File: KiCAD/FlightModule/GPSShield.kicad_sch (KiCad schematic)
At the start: 6 parts

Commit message: コンデンサの容量耐圧が不明なため後ほど調べる
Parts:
- added 1: ~, MKRGPSShield_V4.0:BATT-HOLDER_12MM, symbol MKRGPSShield_V4.0-eagle-import:Arduino-connectors_BATT-HOLDER_12MM
- added C1: ~, MKRGPSShield_V4.0:0402-1005X55N, symbol MKRGPSShield_V4.0-eagle-import:Arduino-rcl_C-0402
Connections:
- net GND: now also 1.P$1 (-), C1.2
- net at IC2.3 (V_BCKP): now also 1.P$2 (+), C1.1

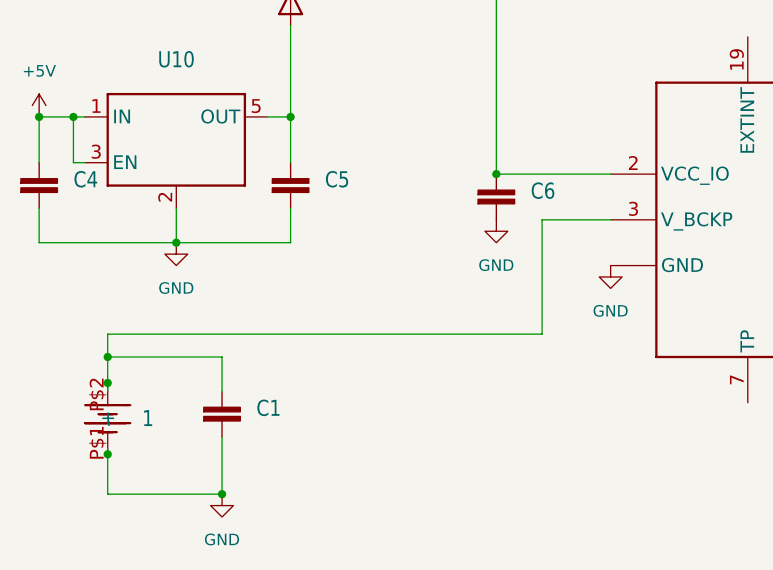
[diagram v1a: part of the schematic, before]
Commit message: MKR周りの配線完了
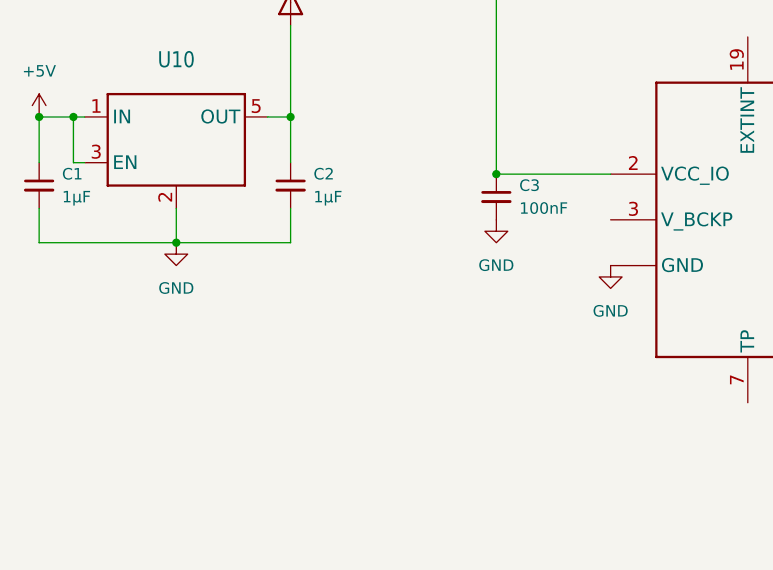
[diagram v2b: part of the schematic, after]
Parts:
- removed 1: ~, MKRGPSShield_V4.0:BATT-HOLDER_12MM, symbol MKRGPSShield_V4.0-eagle-import:Arduino-connectors_BATT-HOLDER_12MM
- removed C1, C4, C5, C6: ~, MKRGPSShield_V4.0:0402-1005X55N, symbol MKRGPSShield_V4.0-eagle-import:Arduino-rcl_C-0402
- added C1, C2: 1μF, symbol Device:C_Small
- added C3: 100nF, symbol Device:C_Small
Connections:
- net +5V: now also C1.1
- net GND: now also C1.2, C2.2, C3.2
- net at D6.2 (A2), U10.5 (OUT): now also C2.1
- net at D6.3 (K), IC2.17 (VCC), IC2.2 (VCC_IO): now also C3.1

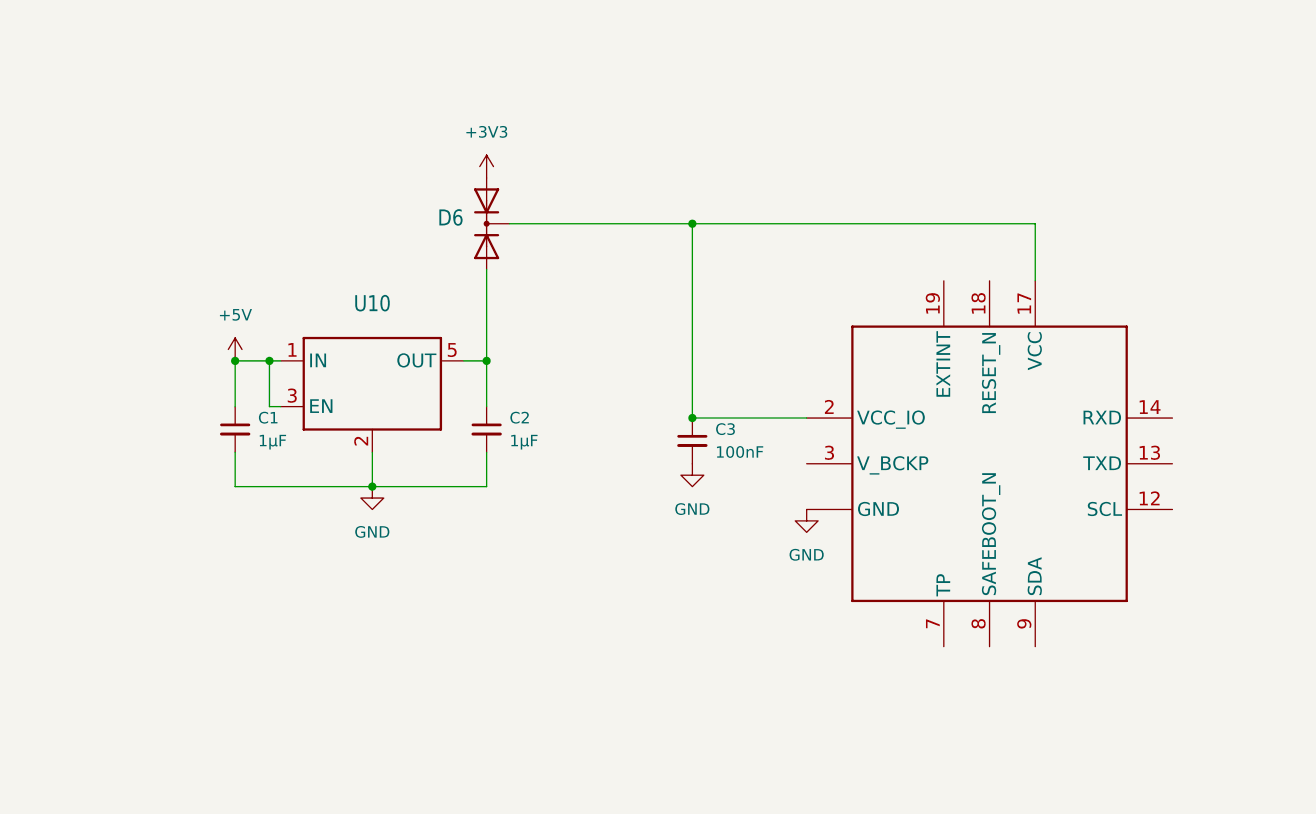
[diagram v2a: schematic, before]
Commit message: GPSShieldの部分完了
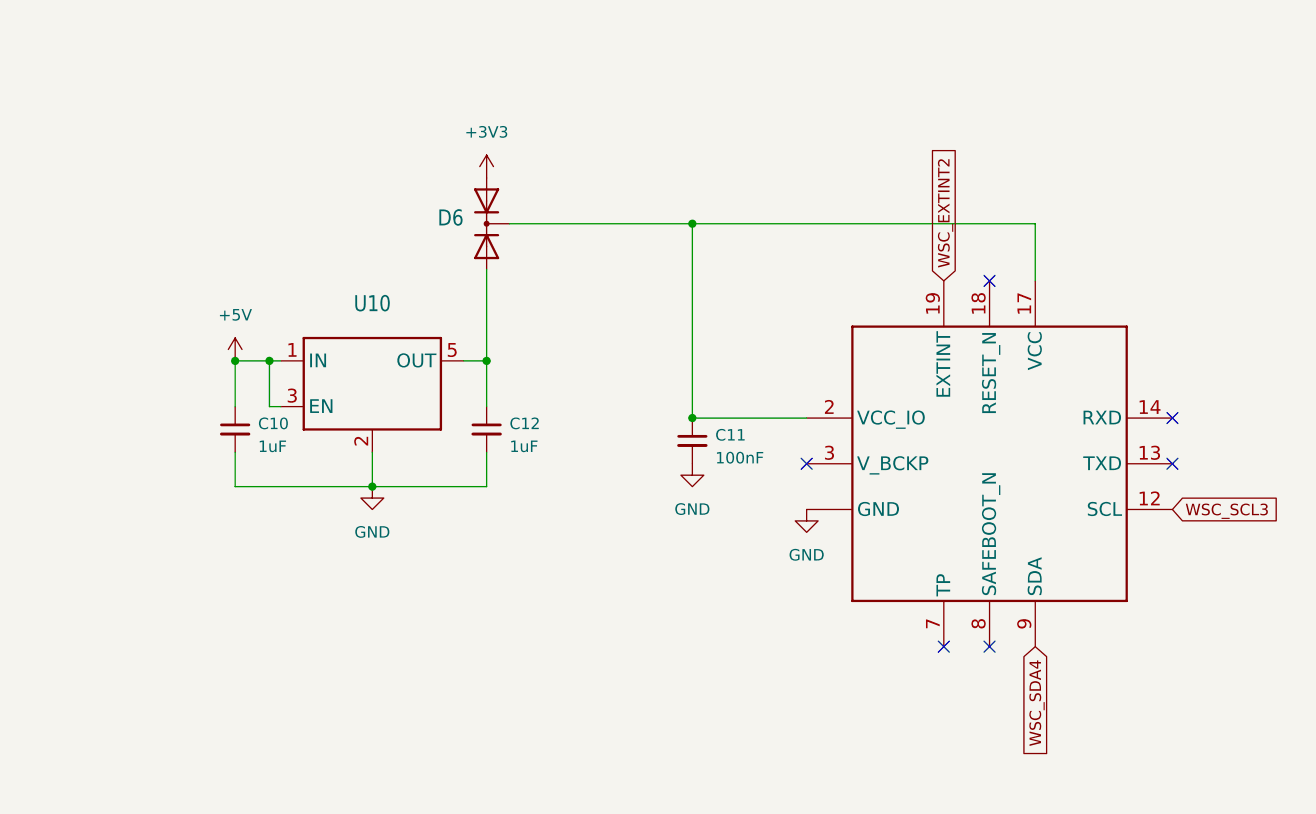
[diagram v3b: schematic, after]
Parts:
- removed C1, C2: 1μF, symbol Device:C_Small
- removed C3: 100nF, symbol Device:C_Small
- added C10, C12: 1uF, Capacitor_SMD:C_1206_3216Metric_Pad1.33x1.80mm_HandSolder, symbol Device:C_Small
- added C11: 100nF, Capacitor_SMD:C_1206_3216Metric_Pad1.33x1.80mm_HandSolder, symbol Device:C_Small
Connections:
- net +5V: now also C10.1
- net GND: now also C10.2, C11.2, C12.2
- net at D6.2 (A2), U10.5 (OUT): now also C12.1
- net at D6.3 (K), IC2.17 (VCC), IC2.2 (VCC_IO): now also C11.1
- net WSC_SCL3: now reaches IC2.12 (SCL)
- net WSC_EXTINT2: now reaches IC2.19 (EXTINT)
- net WSC_SDA4: now reaches IC2.9 (SDA)
- no-connect marks 0 -> 6

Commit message: GNSSモジュール，SAM-M8Qの回路図完成
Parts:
- removed C10, C12: 1uF, Capacitor_SMD:C_1206_3216Metric_Pad1.33x1.80mm_HandSolder, symbol Device:C_Small
- removed C11: 100nF, Capacitor_SMD:C_1206_3216Metric_Pad1.33x1.80mm_HandSolder, symbol Device:C_Small
- removed D6: ~, MKRGPSShield_V4.0:SOT65P210X110-3N, symbol MKRGPSShield_V4.0-eagle-import:Arduino-diodes_A2K_SOT-323
- removed IC2: ~, GPSShield:UBLOXLIB_SAM-M8Q, symbol MKRGPSShield_V4.0-eagle-import:SAM-M8Q
- removed U10: ~, MKRGPSShield_V4.0:SOT25, symbol MKRGPSShield_V4.0-eagle-import:AP2112K-3.3
- added C16, C17: 1uF, Capacitor_SMD:C_1206_3216Metric_Pad1.33x1.80mm_HandSolder, symbol Device:C_Small
- added R27: 100k, Resistor_SMD:R_0603_1608Metric_Pad0.98x0.95mm_HandSolder, symbol Device:R
- added R28: 0, Resistor_SMD:R_0603_1608Metric_Pad0.98x0.95mm_HandSolder, symbol Device:R
- added R29, R30: 4.7k, Resistor_SMD:R_0603_1608Metric_Pad0.98x0.95mm_HandSolder, symbol Device:R
- added U3: SAM-M8Q-0-10, TSRP_IC:MODULE_SAM-M8Q-0-10, symbol TSRP_IC:SAM-M8Q-0-10
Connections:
- net +3V3: now also C16.1, C17.1, R27.1, R28.1, R29.1, R30.1, U3.17 (VCC), U3.2 (VCC_IO)
- net GND: now also C16.2, C17.2, U3.1 (GND), U3.10 (GND), U3.11 (GND), U3.15 (GND), U3.16 (GND), U3.20 (GND), U3.4 (GND), U3.5 (GND), U3.6 (GND)
- new net: R28.2, U3.3 (V_BCKP)
- new net EXTINT_SAM-M8Q: U3.19 (EXTINT0)
- new net I2C_SCL: R29.2, U3.12 (SCL)
- new net I2C_SDA: R30.2, U3.9 (SDA)
- new net UART_RXD: R27.2, U3.14 (RXD)
- new net UART_TXD: U3.13 (TXD)
- no-connect marks 6 -> 2
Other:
- note added: "ジャンパ抵抗"

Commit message: 回路図8割完成
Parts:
- U3: footprint TSRP_IC:MODULE_SAM-M8Q-0-10 -> SAM-M8Q-0-10:MODULE_SAM-M8Q-0-10
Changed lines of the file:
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@@
 			)
 		)
-		(property "Footprint" "TSRP_IC:MODULE_SAM-M8Q-0-10"
+		(property "Footprint" "SAM-M8Q-0-10:MODULE_SAM-M8Q-0-10"
 			(at 104.14 68.58 0)
 			(effects
@@
 				(path "/3507137a-fdd7-4bc0-abe8-370b7c3b390e/5f21eb00-60ce-4306-a223-a9b9ec9552df"
 					(reference "#PWR062")
+					(unit 1)
+				)
+			)
+		)
+	)
+	(symbol
+		(lib_name "GND_2")
+		(lib_id "power:GND")
+		(at 93.98 93.98 0)
+		(unit 1)
+		(exclude_from_sim no)
+		(in_bom yes)
+		(on_board yes)
+		(dnp no)
+		(fields_autoplaced yes)
+		(property "Reference" "#PWR014"
+			(at 93.98 100.33 0)
+			(effects
+				(font
+					(size 1.27 1.27)
+				)
+				(hide yes)
+			)
+		)
+		(property "Value" "GND"
+			(at 93.98 99.06 0)
+			(effects
+				(font
+					(size 1.27 1.27)
+				)
+			)
+		)
+		(property "Footprint" ""
+			(at 93.98 93.98 0)
+			(effects
+				(font
+					(size 1.27 1.27)
+				)
+				(hide yes)
+			)
+		)
+		(property "Datasheet" ""
+			(at 93.98 93.98 0)
+			(effects
+				(font
+					(size 1.27 1.27)
+				)
+				(hide yes)
+			)
+		)
+		(property "Description" "Power symbol creates a global label with name \"GND\" , ground"
+			(at 93.98 93.98 0)
+			(effects
+				(font
+					(size 1.27 1.27)
+				)
+				(hide yes)
+			)
+		)
+		(pin "1"
+		)
+		(instances
+			(project "FlightModule"
+				(path "/3507137a-fdd7-4bc0-abe8-370b7c3b390e/5f21eb00-60ce-4306-a223-a9b9ec9552df"
+					(reference "#PWR014")
+					(unit 1)
+				)
+			)
+			(project "GPSShield"
+				(path "/e91f5324-b1bd-4996-81c2-18550b5297b9"
+					(reference "#PWR?")
 					(unit 1)
 				)
@@
 					(unit 1)
 				)
-			)
-		)
-	)
-	(symbol
-		(lib_name "GND_2")
-		(lib_id "power:GND")
-		(at 93.98 93.98 0)
-		(unit 1)
-		(exclude_from_sim no)
-		(in_bom yes)
-		(on_board yes)
-		(dnp no)
-		(fields_autoplaced yes)
-		(property "Reference" "#PWR014"
-			(at 93.98 100.33 0)
-			(effects
-				(font
-					(size 1.27 1.27)
-				)
-				(hide yes)
-			)
-		)
-		(property "Value" "GND"
-			(at 93.98 99.06 0)
-			(effects
-				(font
-					(size 1.27 1.27)
-				)
-			)
-		)
-		(property "Footprint" ""
-			(at 93.98 93.98 0)
-			(effects
-				(font
-					(size 1.27 1.27)
-				)
-				(hide yes)
-			)
-		)
-		(property "Datasheet" ""
-			(at 93.98 93.98 0)
-			(effects
-				(font
-					(size 1.27 1.27)
-				)
-				(hide yes)
-			)
-		)
-		(property "Description" "Power symbol creates a global label with name \"GND\" , ground"
-			(at 93.98 93.98 0)
-			(effects
-				(font
-					(size 1.27 1.27)
-				)
-				(hide yes)
-			)
-		)
-		(pin "1"
-		)
-		(instances
-			(project "FlightModule"
-				(path "/3507137a-fdd7-4bc0-abe8-370b7c3b390e/5f21eb00-60ce-4306-a223-a9b9ec9552df"
-					(reference "#PWR014")
-					(unit 1)
-				)
-			)
-			(project "GPSShield"
-				(path "/e91f5324-b1bd-4996-81c2-18550b5297b9"
-					(reference "#PWR?")
-					(unit 1)
-				)

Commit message: 配線8割り終わり．次の作業....
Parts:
- U3: footprint SAM-M8Q-0-10:MODULE_SAM-M8Q-0-10 -> TSRP_IC:MODULE_SAM-M8Q-0-10
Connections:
- net +3V3 renamed +3.3V

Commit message: 最終確認終わり
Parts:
- C16, C17: footprint Capacitor_SMD:C_1206_3216Metric_Pad1.33x1.80mm_HandSolder -> Capacitor_SMD:C_0805_2012Metric_Pad1.18x1.45mm_HandSolder
- R27: value 100k -> 100kR
- R28: value 0 -> 0R
- R29, R30: value 4.7k -> 4.7kR
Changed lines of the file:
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@@
 			)
 		)
-		(property "Footprint" "Capacitor_SMD:C_1206_3216Metric_Pad1.33x1.80mm_HandSolder"
+		(property "Footprint" "Capacitor_SMD:C_0805_2012Metric_Pad1.18x1.45mm_HandSolder"
 			(at 152.4 45.72 0)
 			(effects
@@
 			)
 		)
-		(property "Datasheet" "https://akizukidenshi.com/catalog/g/gP-17338/"
+		(property "Datasheet" "https://akizukidenshi.com/catalog/g/g113699/"
 			(at 152.4 45.72 0)
 			(effects
@@
 			)
 		)
-		(property "Value" "4.7k"
+		(property "Value" "4.7kR"
 			(at 53.34 67.3099 0)
 			(effects
@@
 			)
 		)
-		(property "Value" "4.7k"
+		(property "Value" "4.7kR"
 			(at 43.18 67.3099 0)
 			(effects
@@
 			)
 		)
-		(property "Footprint" "Capacitor_SMD:C_1206_3216Metric_Pad1.33x1.80mm_HandSolder"
+		(property "Footprint" "Capacitor_SMD:C_0805_2012Metric_Pad1.18x1.45mm_HandSolder"
 			(at 100.33 40.64 0)
 			(effects
@@
 			)
 		)
-		(property "Datasheet" "https://akizukidenshi.com/catalog/g/gP-17338/"
+		(property "Datasheet" "https://akizukidenshi.com/catalog/g/g113699/"
 			(at 100.33 40.64 0)
 			(effects
@@
 			)
 		)
-		(property "Value" "100k"
+		(property "Value" "100kR"
 			(at 143.51 67.3099 0)
 			(effects
@@
 			)
 		)
-		(property "Value" "0"
+		(property "Value" "0R"
 			(at 128.27 50.7999 0)
 			(effects
